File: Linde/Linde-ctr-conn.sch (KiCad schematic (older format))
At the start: 8 parts, among them P1 CONN_SbS_02X08, SW1.1 SW_Push_Open_Dual, SW1.2 SW_Push, SW1.? SW_Push

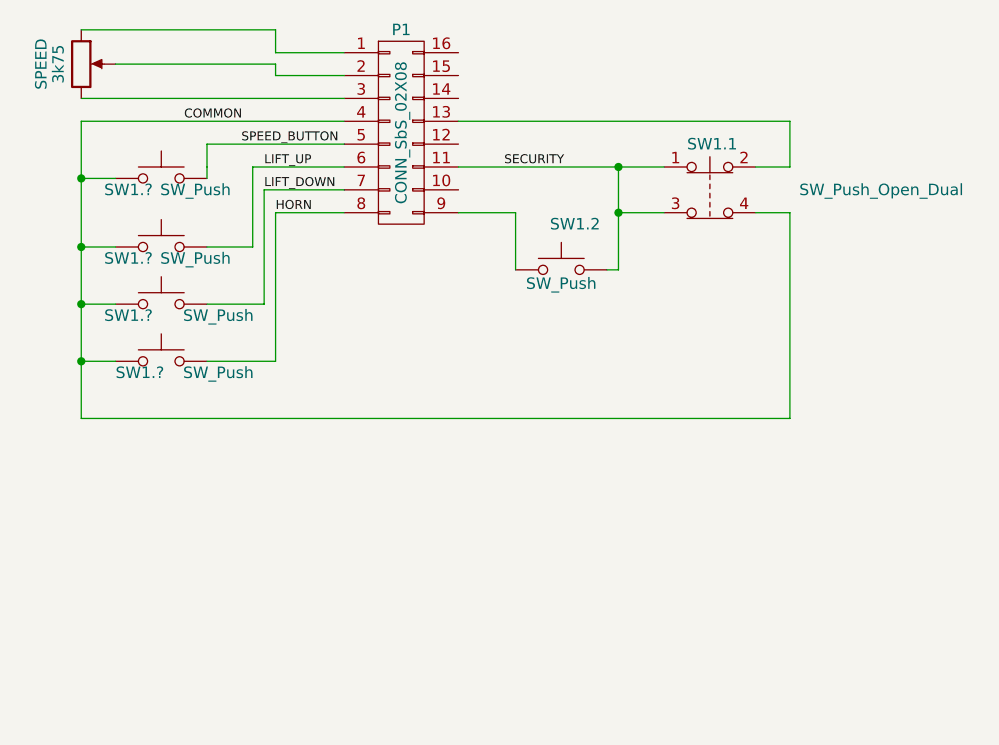
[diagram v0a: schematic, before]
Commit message: Steering added
Steering wheel connector added
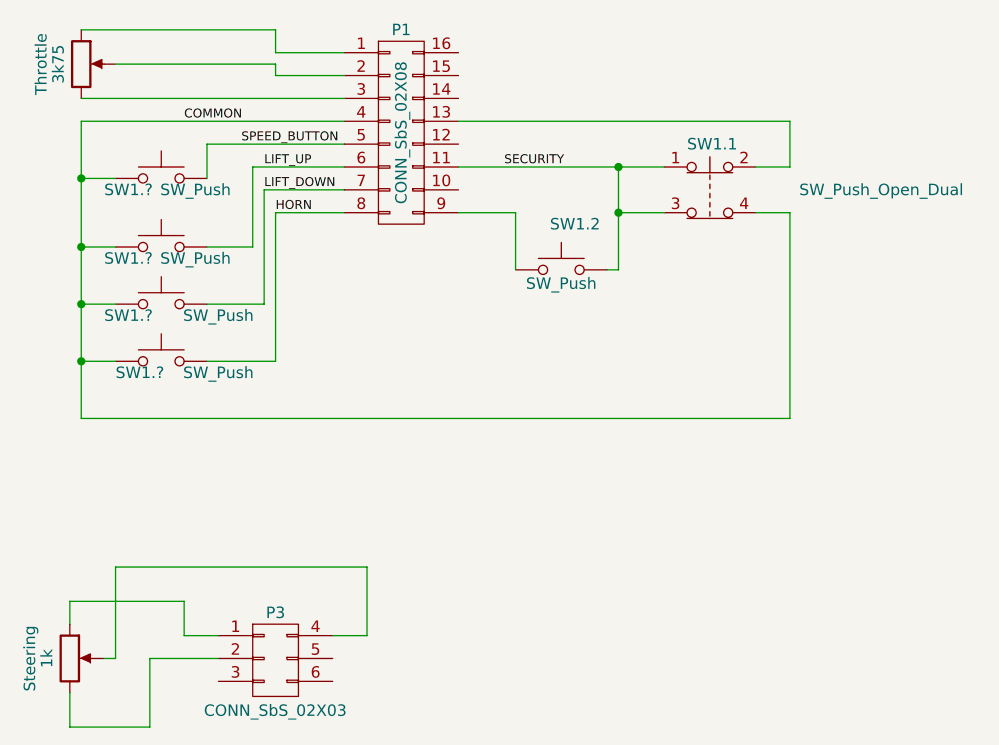
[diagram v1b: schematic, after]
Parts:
- added P3: CONN_SbS_02X03, symbol CONN_SbS_02X03
- added Steering: 1k, symbol POT
- renumbered SPEED to Throttle
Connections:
- new net: P3.1 (P1), Steering.1
- new net: P3.2 (P2), Steering.3
- new net: P3.4 (P4), Steering.2
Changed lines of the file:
@@
 LIBS:conn_sbs_02x08
 LIBS:switches
-LIBS:Linde-cache
 EELAYER 25 0
 EELAYER END
@@
 	1900 2450 3050 2450
 $Comp
-L POT SPEED
+L POT Throttle
 U 1 1 58C12E46
 P 1900 2300
-F 0 "SPEED" V 1725 2300 50  0000 C CNN
+F 0 "Throttle" V 1725 2300 50  0000 C CNN
 F 1 "3k75" V 1800 2300 50  0000 C CNN
 F 2 "" H 1900 2300 50  0000 C CNN
@@
 	3050 2550 1900 2550
 Wire Wire Line
-	1900 2550 1900 2800
-Wire Wire Line
-	1900 2800 1900 3100
-Wire Wire Line
-	1900 3100 1900 3350
-Wire Wire Line
-	1900 3350 1900 3600
-Wire Wire Line
-	1900 3600 1900 3850
+	1900 2550 1900 3850
 Text Label 2600 2650 0    39   ~ 0
 SPEED_BUTTON
@@
 	3550 2550 5000 2550
 Wire Wire Line
-	3550 2750 4250 2750
-Wire Wire Line
-	4250 2750 4450 2750
+	3550 2750 4450 2750
 Text Label 3750 2750 0    39   ~ 0
 SECURITY
@@
 $EndComp
 Wire Wire Line
-	4250 2750 4250 2950
-Wire Wire Line
-	4250 2950 4250 3200
+	4250 2750 4250 3200
 Wire Wire Line
 	4250 2950 4450 2950
@@
 	2650 2750 2650 3100
 Wire Wire Line
-	2450 2800 2450 2750
+	2450 2650 2450 2800
 Wire Wire Line
 	3050 2650 2450 2650
-Wire Wire Line
-	2450 2650 2450 2750
 Wire Wire Line
 	2050 2800 1900 2800
 Connection ~ 1900 2800
+$Comp
+L CONN_SbS_02X03 P3
+U 1 1 58C28F6B
+P 2750 4900
+F 0 "P3" H 2750 5100 50  0000 C CNN
+F 1 "CONN_SbS_02X03" H 2749 4672 50  0000 C CNN
+F 2 "" H 2750 3700 50  0000 C CNN
+F 3 "" H 2750 3700 50  0000 C CNN
+	1    2750 4900
+	1    0    0    -1
+$EndComp
+$Comp
+L POT Steering
+U 1 1 58C2924E
+P 1850 4900
+F 0 "Steering" V 1675 4900 50  0000 C CNN
+F 1 "1k" V 1750 4900 50  0000 C CNN
+F 2 "" H 1850 4900 50  0000 C CNN
+F 3 "" H 1850 4900 50  0000 C CNN
+	1    1850 4900
+	1    0    0    -1
+$EndComp
+Wire Wire Line
+	2500 4800 2350 4800
+Wire Wire Line
+	2350 4800 2350 4650
+Wire Wire Line
+	2350 4650 1850 4650
+Wire Wire Line
+	1850 4650 1850 4750
+Wire Wire Line
+	2500 4900 2200 4900
+Wire Wire Line
+	2200 4900 2200 5200
+Wire Wire Line
+	2200 5200 1850 5200
+Wire Wire Line
+	1850 5200 1850 5050
+Wire Wire Line
+	3000 4800 3150 4800
+Wire Wire Line
+	3150 4800 3150 4500
+Wire Wire Line
+	3150 4500 2050 4500
+Wire Wire Line
+	2050 4500 2050 4900
+Wire Wire Line
+	2050 4900 2000 4900
 $EndSCHEMATC
